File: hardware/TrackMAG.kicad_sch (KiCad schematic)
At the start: 48 parts, among them J1 USB_C_Socket_USB2.0, J2 Conn_Debug, SW1 SW_RESET, SW2 SW_BOOT0, U1 LSM6DS3TR-C, U2 USBLC6-2P6, U3 STM32F103C8T6, U4 LIS2MDLTR, U5 AMS1117-3.3, Y1 16MHz

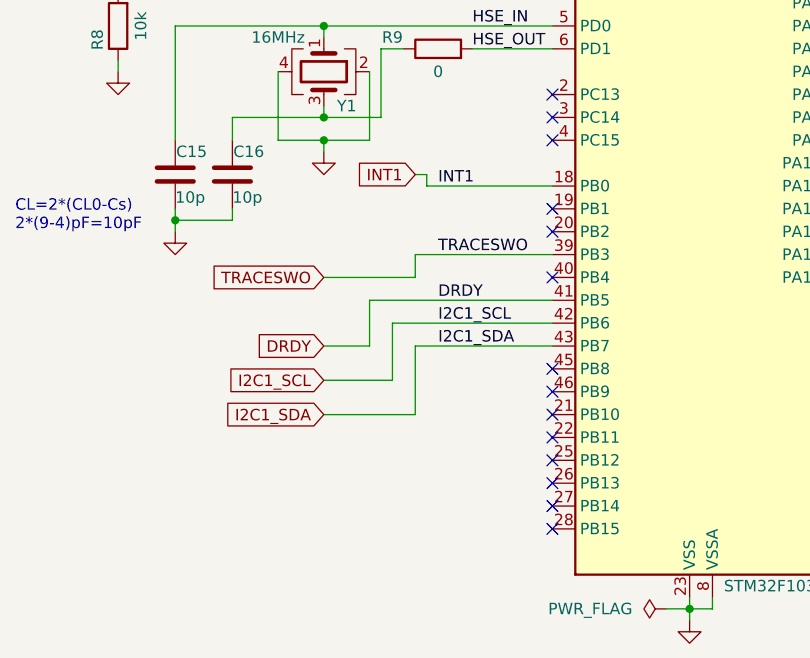
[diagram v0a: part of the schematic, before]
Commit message: Update pinout to match current firmware configuration
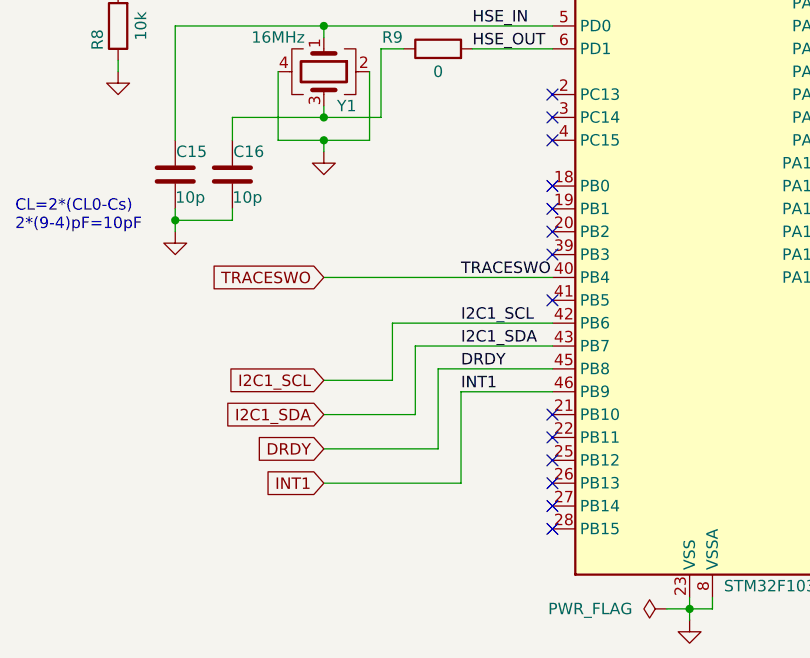
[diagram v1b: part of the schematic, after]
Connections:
- net DRDY: now also U3.45 (PB8); no longer U3.41 (PB5)
- net INT1: now also U3.46 (PB9); no longer U3.18 (PB0)
- net TRACESWO: now also U3.40 (PB4); no longer U3.39 (PB3)

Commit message: Backup current progress
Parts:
- removed C18: 10n, Capacitor_SMD:C_0402_1005Metric, symbol Device:C
- removed C19, C20: 1u, Capacitor_SMD:C_0402_1005Metric, symbol Device:C
- removed FB2: 100R, Resistor_SMD:R_0805_2012Metric, symbol Device:FerriteBead
- removed U1: LSM6DS3TR-C, Package_LGA:LGA-14_3x2.5mm_P0.5mm_LayoutBorder3x4y, symbol TrackMAG:LSM6DS3TR-C
- removed U4: LIS2MDLTR, Package_LGA:LGA-12_2x2mm_P0.5mm, symbol TrackMAG:LIS2MDLTR
- added D1: LED, LED_SMD:LED_0603_1608Metric, symbol Device:LED
- added H1, H2, H3: MountingHole, MountingHole:MountingHole_2.1mm, symbol Mechanical:MountingHole
- added U1: LSM6DS3TR-C, TrackMAG:LGA-14_3x2.5mm_P0.5mm_LayoutBorder3x4y, symbol Sensor_Motion:LSM6DS3
- added U4: LIS2MDL, TrackMAG:LGA-12_2x2mm_P0.5mm, symbol Sensor_Magnetic:LIS2MDL
- C1, C10, C11, C12, C13, C14, C15, C16, C17, C2, C3, C4, C5, C6, C7, C8, C9: footprint Capacitor_SMD:C_0402_1005Metric -> TrackMAG:C_0402_1005Metric
- J1: footprint Connector_USB:USB_C_Receptacle_G-Switch_GT-USB-7010ASV -> TrackMAG:USB_C_Receptacle_G-Switch_GT-USB-7010ASV
- J2: footprint Connector_PinHeader_2.54mm:PinHeader_1x05_P2.54mm_Vertical -> TrackMAG:PinHeader_1x05_P2.54mm_Debug
- R1, R10, R11, R12, R2, R3, R4, R5, R6: footprint Resistor_SMD:R_0402_1005Metric -> TrackMAG:R_0402_1005Metric
- R13: value 0 -> 1k5; footprint Resistor_SMD:R_0402_1005Metric -> TrackMAG:R_0402_1005Metric; JLCPCB Part # C17168 -> C25867
- R7: renamed from R8; footprint Resistor_SMD:R_0402_1005Metric -> TrackMAG:R_0402_1005Metric
- R8: renamed from R9; footprint Resistor_SMD:R_0402_1005Metric -> TrackMAG:R_0402_1005Metric
- R9: renamed from R7; footprint Resistor_SMD:R_0402_1005Metric -> TrackMAG:R_0402_1005Metric
- SW1, SW2: footprint Button_Switch_SMD:SW_Push_1P1T_XKB_TS-1187A -> TrackMAG:SW_Push_1P1T_XKB_TS-1187A
- U2: footprint Package_TO_SOT_SMD:SOT-666 -> TrackMAG:SOT-666
- renumbered C21 to C18, C22 to C19, D1 to D2
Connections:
- net +3.3V: now also C19.1, U5.2 (VO), D1.2 (A), U1.12 (CS), U1.5 (VDDIO), U1.8 (VDD), U4.10 (Vdd_IO), U4.3 (~{CS}), U4.9 (Vdd)
- net DRDY: now also U4.7 (DRDY)
- net GND: now also J1.S1 (SHIELD), R13.2, U1.6 (GND), U1.7 (GND), U4.6 (GND), U4.8 (GND); no longer R13.1
- net HSE_OUT: now also C16.1, R8.1, Y1.3; no longer R8.2, U3.6 (PD1)
- net I2C_SCX: now also U1.3 (SCX), U4.1 (SCL/SPC)
- net I2C_SDX: now also U1.2 (SDX), U4.4 (SDA/SDI/SDO)
- net INT1: now also U1.4 (INT1)
- net USB_D+: now also U2.3 (I/O2); no longer U2.1 (I/O1)
- net USB_D-: now also U2.4 (I/O2); no longer U2.6 (I/O1)
- net INT2: now reaches R9.2
- net INT2: now also U1.9 (INT2)
- net CC2: now reaches J1.B5 (CC2), R6.2
- net CC1: now reaches J1.A5 (CC1), R5.2
- net US_D+: now reaches J1.A6 (D+), J1.B6 (D+)
- net US_D+: now also U2.1 (I/O1); no longer U2.3 (I/O2)
- net US_D-: now reaches J1.A7 (D-), J1.B7 (D-)
- net US_D-: now also U2.6 (I/O1); no longer U2.4 (I/O2)
- net at R4.1: now also U1.1 (SDO/SA0)
- net C1: now reaches C17.1
- net C1: now also U4.5 (C1)
- net I2C2_SCL: now reaches U3.21 (PB10)
- net I2C2_SCL: now also U1.13 (SCL)
- net I2C2_SDA: now reaches U3.22 (PB11)
- net I2C2_SDA: now also R3.1, U1.14 (SDA)
- net I2C1_SCL: no longer names the net of U3.42 (PB6)
- net I2C1_SDA: no longer names the net of U3.43 (PB7)
- net I2C1_SDA: no longer R3.1
- new net: D1.1 (K), R13.1
- new net HSE_O: R8.2, U3.6 (PD1)
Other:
- note added: "Mounting Holes"
- moved on the sheet: C15, C16, C17, C18, C19, J1, R7, R8, R9, Y1

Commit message: Backup currend KiCAD progress
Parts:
- removed C5: 10u, TrackMAG:C_0402_1005Metric, symbol Device:C
- removed R9: 0, TrackMAG:R_0402_1005Metric, symbol Device:R
- removed U1: LSM6DS3TR-C, TrackMAG:LGA-14_3x2.5mm_P0.5mm_LayoutBorder3x4y, symbol Sensor_Motion:LSM6DS3
- removed U2: USBLC6-2P6, TrackMAG:SOT-666, symbol Power_Protection:USBLC6-2P6
- added C1, C2, C3: 1u, TrackMAG:C_0402_1005Metric, symbol Device:C
- added C18, C8: 10u, Capacitor_Tantalum_SMD:CP_EIA-3216-18_Kemet-A, symbol Device:C_Polarized
- added C19: 100n, TrackMAG:C_0402_1005Metric, symbol Device:C
- added C20: 10n, TrackMAG:C_0402_1005Metric, symbol Device:C
- added FB2: 100R, Resistor_SMD:R_0805_2012Metric, symbol Device:FerriteBead
- added U1: LSM6DS3TR-C, TrackMAG:LGA-14_3x2.5mm_P0.5mm_LayoutBorder3x4y, symbol LSM6DS3TR-C:LSM6DS3TR-C
- added U2: USBLC6-2P6, TrackMAG:SOT-666, symbol USBLC6-2P:USBLC6-2P6
- SW1: footprint TrackMAG:SW_Push_1P1T_XKB_TS-1187A -> TrackMAG:SW_Push_1P1T_XKB_TS-1187A_RESET
- SW2: value SW_BOOT0 -> SW_BOOT; footprint TrackMAG:SW_Push_1P1T_XKB_TS-1187A -> TrackMAG:SW_Push_1P1T_XKB_TS-1187A_BOOT
- renumbered C7 to C10, C8 to C11, C9 to C12, C10 to C13, C11 to C14, C12 to C15, C13 to C16, C14 to C17, C15 to C21, C16 to C22, C17 to C23, C18 to C24, C19 to C25, C1 to C4, C2 to C5, C3 to C6, C4 to C7, C6 to C9
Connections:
- net +3.3V: now also C1.1, C2.1, C3.1, C8.1, U1.12 (CS), U1.5 (VDDIO), U1.8 (VDD)
- net GND: now also J2.4 (Pin_4), C1.2, C18.2, C19.2, C2.2, C20.2, C3.2, C8.2, U1.6 (GND), U1.7 (GND), U1.9 (INT2), U2.2 (GND); no longer J2.5 (Pin_5)
- net I2C2_SCL: now also R2.1, U1.13 (SCL)
- net I2C2_SDA: now also U1.14 (SDA)
- net I2C_SCX: now also U1.3 (SCX); no longer R2.1
- net I2C_SDX: now also U1.2 (SDX)
- net INT1: now also U3.16 (PA6), U1.4 (INT1); no longer U3.46 (PB9)
- net RESET: now also J2.1 (Pin_1); no longer J2.4 (Pin_4)
- net SWCLK: now also J2.3 (Pin_3); no longer J2.2 (Pin_2)
- net SWDIO: now also J2.5 (Pin_5); no longer J2.1 (Pin_1)
- net USB_D+: now also U2.6 (I/O1)
- net USB_D-: now also U2.1 (I/O1)
- net US_D+: now also U2.4 (I/O2)
- net US_D-: now also U2.3 (I/O2)
- net VBUS: now also C18.1, C19.1, FB2.1; no longer C24.1, D2.1 (A1), U5.3 (VI)
- net at R4.1: now also U1.1 (SDO/SA0)
- net TRACESWO renamed SWO
- net SWO: now also J2.2 (Pin_2); no longer J2.3 (Pin_3)
- new net +5V: C20.1, C24.1, D2.1 (A1), FB2.2, U2.5 (VBUS), U5.3 (VI)
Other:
- note added: "Decouling caps LIS2MDL"
- note added: "Decoupling caps LSM6DS3TR-C"
- note added: "Extra caps due to high ESR of C8"
- moved on the sheet: R2, R3

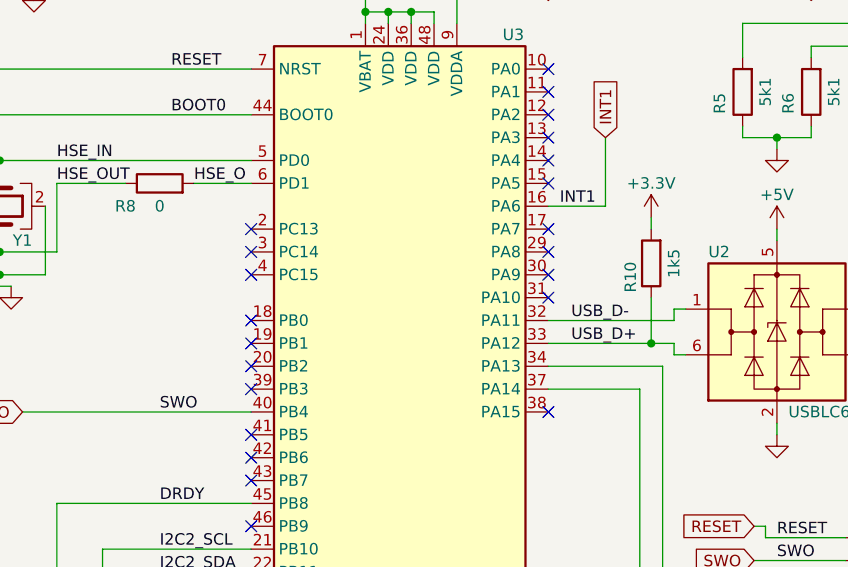
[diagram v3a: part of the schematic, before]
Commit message: Add missing connections
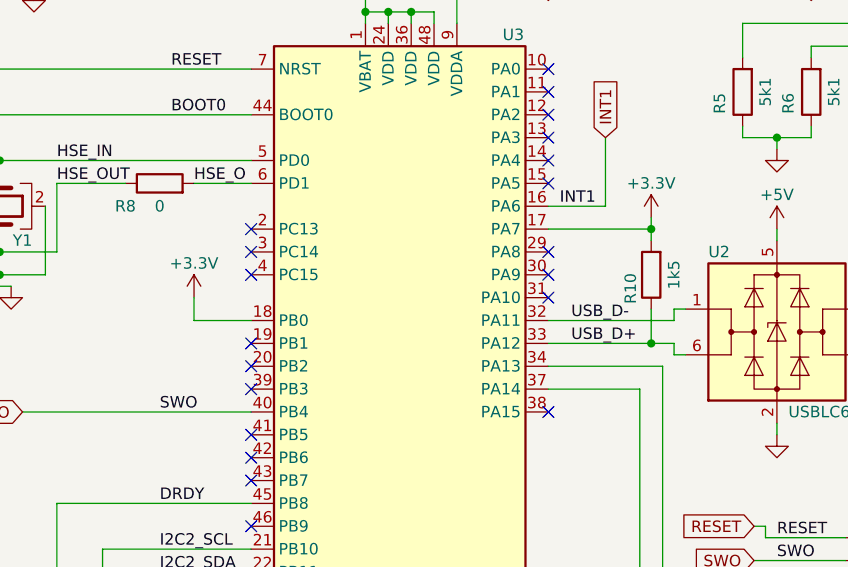
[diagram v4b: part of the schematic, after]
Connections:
- net +3.3V: now also U3.17 (PA7), U3.18 (PB0)
- no-connect marks 28 -> 26
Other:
- moved on the sheet: R10
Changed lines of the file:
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@@
   (junction (at 96.52 46.99) (diameter 0) (color 0 0 0 0)
+  )
+  (junction (at 134.62 86.36) (diameter 0) (color 0 0 0 0)
   )
   (junction (at 53.34 181.61) (diameter 0) (color 0 0 0 0)
@@
   (no_connect (at 90.17 101.6))
   (no_connect (at 90.17 86.36))
-  (no_connect (at 90.17 96.52))
   (no_connect (at 90.17 99.06))
   (no_connect (at 123.19 81.28))
@@
   (no_connect (at 123.19 88.9))
   (no_connect (at 90.17 127))
-  (no_connect (at 123.19 86.36))
   (no_connect (at 90.17 111.76))
   (no_connect (at 90.17 134.62))
@@
     (stroke (width 0) (type default))
   )
+  (wire (pts (xy 134.62 86.36) (xy 134.62 87.63))
+    (stroke (width 0) (type default))
+  )
   (wire (pts (xy 251.46 90.17) (xy 251.46 92.71))
     (stroke (width 0) (type default))
@@
     (stroke (width 0) (type default))
   )
-  (wire (pts (xy 134.62 93.98) (xy 134.62 99.06))
+  (wire (pts (xy 134.62 95.25) (xy 134.62 99.06))
     (stroke (width 0) (type default))
   )
@@
     (stroke (width 0) (type default))
   )
+  (wire (pts (xy 123.19 86.36) (xy 134.62 86.36))
+    (stroke (width 0) (type default))
+  )
   (wire (pts (xy 251.46 130.81) (xy 251.46 132.08))
     (stroke (width 0) (type default))
@@
     (stroke (width 0) (type default))
   )
+  (wire (pts (xy 83.82 93.98) (xy 83.82 96.52))
+    (stroke (width 0) (type default))
+  )
   (wire (pts (xy 53.34 171.45) (xy 55.88 171.45))
     (stroke (width 0) (type default))
@@
   )
   (wire (pts (xy 144.78 63.5) (xy 160.02 63.5))
+    (stroke (width 0) (type default))
+  )
+  (wire (pts (xy 83.82 96.52) (xy 90.17 96.52))
     (stroke (width 0) (type default))
   )
@@
     )
   )
-  (symbol (lib_id "Device:R") (at 134.62 90.17 180) (unit 1)
-    (in_bom yes) (on_board yes) (dnp no)
-    (property "Reference" "R10" (at 132.334 91.694 90)
-      (effects (font (size 1.27 1.27)))
-    )
-    (property "Value" "1k5" (at 137.16 90.17 90)
-      (effects (font (size 1.27 1.27)))
-    )
-    (property "Footprint" "TrackMAG:R_0402_1005Metric" (at 136.398 90.17 90)
-      (effects (font (size 1.27 1.27)) hide)
-    )
-    (property "Datasheet" "~" (at 134.62 90.17 0)
-      (effects (font (size 1.27 1.27)) hide)
-    )
-    (property "JLCPCB Part #" "C25867" (at 134.62 90.17 90)
+  (symbol (lib_id "Device:R") (at 134.62 91.44 180) (unit 1)
+    (in_bom yes) (on_board yes) (dnp no)
+    (property "Reference" "R10" (at 132.334 92.964 90)
+      (effects (font (size 1.27 1.27)))
+    )
+    (property "Value" "1k5" (at 137.16 91.44 90)
+      (effects (font (size 1.27 1.27)))
+    )
+    (property "Footprint" "TrackMAG:R_0402_1005Metric" (at 136.398 91.44 90)
+      (effects (font (size 1.27 1.27)) hide)
+    )
+    (property "Datasheet" "~" (at 134.62 91.44 0)
+      (effects (font (size 1.27 1.27)) hide)
+    )
+    (property "JLCPCB Part #" "C25867" (at 134.62 91.44 90)
       (effects (font (size 1.27 1.27)) hide)
     )
@@
         )
       )
+    )
+  )
+  (symbol (lib_id "power:+3.3V") (at 83.82 93.98 0) (unit 1)
+    (in_bom yes) (on_board yes) (dnp no)
+    (property "Reference" "#PWR035" (at 83.82 97.79 0)
+      (effects (font (size 1.27 1.27)) hide)
+    )
+    (property "Value" "+3.3V" (at 83.82 90.17 0)
+      (effects (font (size 1.27 1.27)))
+    )
+    (property "Footprint" "" (at 83.82 93.98 0)
+      (effects (font (size 1.27 1.27)) hide)
+    )
+    (property "Datasheet" "" (at 83.82 93.98 0)
+      (effects (font (size 1.27 1.27)) hide)
+    )
+    (pin "1")
+    (instances
+      (project "TrackMAG"
+        (path "/caace321-8fd3-459f-935a-1c27778b7f28"
+          (reference "#PWR035") (unit 1)
+        )
+      )

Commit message: Cleanup
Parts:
- D1: JLCPCB Part # (none) -> C2286
- H1, H2, H3: now left out of the parts list
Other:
- note added: "Extra caps due to high ESR of C8 (3Ω)"
- note removed: "Extra caps due to high ESR of C8"
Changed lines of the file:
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@@
     (effects (font (size 2.54 2.54) bold) (justify left bottom))
   )
-  (text "Extra caps due to\nhigh ESR of C8" (at 203.2 43.18 0)
+  (text "Extra caps due to\nhigh ESR of C8 (3Ω)" (at 203.2 43.18 0)
     (effects (font (size 1.27 1.27)) (justify left bottom))
   )
@@
   )
   (symbol (lib_id "Mechanical:MountingHole") (at 90.17 172.72 0) (unit 1)
-    (in_bom yes) (on_board yes) (dnp no) (fields_autoplaced)
+    (in_bom no) (on_board yes) (dnp no) (fields_autoplaced)
     (property "Reference" "H2" (at 92.71 171.45 0)
       (effects (font (size 1.27 1.27)) (justify left))
@@
   )
   (symbol (lib_id "Mechanical:MountingHole") (at 90.17 166.37 0) (unit 1)
-    (in_bom yes) (on_board yes) (dnp no) (fields_autoplaced)
+    (in_bom no) (on_board yes) (dnp no) (fields_autoplaced)
     (property "Reference" "H1" (at 92.71 165.1 0)
       (effects (font (size 1.27 1.27)) (justify left))
@@
   )
   (symbol (lib_id "Device:LED") (at 59.69 171.45 180) (unit 1)
-    (in_bom yes) (on_board yes) (dnp no) (fields_autoplaced)
-    (property "Reference" "D1" (at 61.2775 163.83 0)
-      (effects (font (size 1.27 1.27)))
-    )
-    (property "Value" "LED" (at 61.2775 166.37 0)
-      (effects (font (size 1.27 1.27)))
+    (in_bom yes) (on_board yes) (dnp no)
+    (property "Reference" "D1" (at 59.69 168.91 0)
+      (effects (font (size 1.27 1.27)))
+    )
+    (property "Value" "LED" (at 59.69 168.91 0)
+      (effects (font (size 1.27 1.27)) hide)
     )
     (property "Footprint" "LED_SMD:LED_0603_1608Metric" (at 59.69 171.45 0)
@@
     )
     (property "Datasheet" "~" (at 59.69 171.45 0)
+      (effects (font (size 1.27 1.27)) hide)
+    )
+    (property "JLCPCB Part #" "C2286" (at 59.69 171.45 0)
       (effects (font (size 1.27 1.27)) hide)
     )
@@
   )
   (symbol (lib_id "Mechanical:MountingHole") (at 90.17 179.07 0) (unit 1)
-    (in_bom yes) (on_board yes) (dnp no) (fields_autoplaced)
+    (in_bom no) (on_board yes) (dnp no) (fields_autoplaced)
     (property "Reference" "H3" (at 92.71 177.8 0)
       (effects (font (size 1.27 1.27)) (justify left))

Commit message: Add calibrate switch
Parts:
- added C23: 100n, TrackMAG:C_0402_1005Metric, symbol Device:C
- added R12: 10k, TrackMAG:R_0402_1005Metric, symbol Device:R
- added SW3: SW_CALIBRATE, TrackMAG:SW_Push_1P1T_XKB_TS-1187A_CALIBRATE, symbol Switch:SW_Push
- renumbered C23 to C24, C24 to C25, C25 to C26, R11 to R10, R12 to R11, R10 to R9
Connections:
- net +3.3V: now also R12.2
- net GND: now also C23.2, SW3.1
- net CALIBRATE: now reaches U3.11 (PA1)
- net CALIBRATE: now also C23.1, R12.1, SW3.2
- no-connect marks 26 -> 25

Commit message: Fix various problems, cleanup after review
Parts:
- removed U2: USBLC6-2P6, TrackMAG:SOT-666, symbol USBLC6-2P:USBLC6-2P6
- added U2: USBLC6-2P6, TrackMAG:SOT-666, symbol Power_Protection:USBLC6-2P6
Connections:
- net +5V: now also U2.5 (VBUS)
- net GND: now also U2.2 (GND)
- net USB_D+: now also U2.4 (I/O2)
- net USB_D-: now also U2.6 (I/O1)
- net US_D+ renamed U_D+
- net U_D+: now also U2.3 (I/O2)
- net US_D- renamed U_D-
- net U_D-: now also U2.1 (I/O1)
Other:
- moved on the sheet: R9
